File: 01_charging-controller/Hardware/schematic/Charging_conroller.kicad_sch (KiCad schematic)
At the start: 22 parts, among them J1 CAN, J2 SWD, J7 Conn_01x03, J8 Conn_01x03, J9 Conn_01x01, U1 STM32F103CBTx, U2 MCP2562-E-P, U3 L78L33_TO92

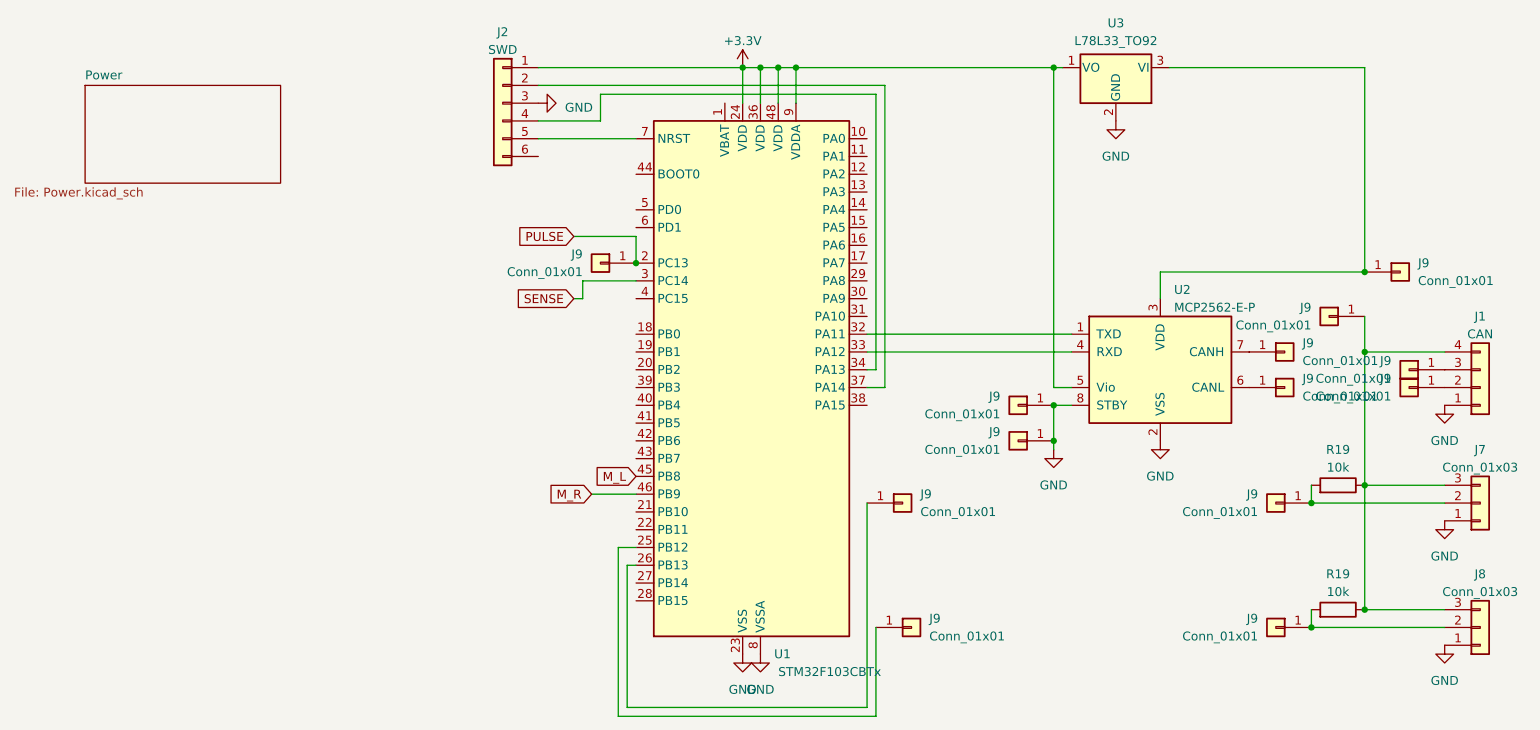
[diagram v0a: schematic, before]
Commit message: minor mistakes fixed; reflected hardware updates
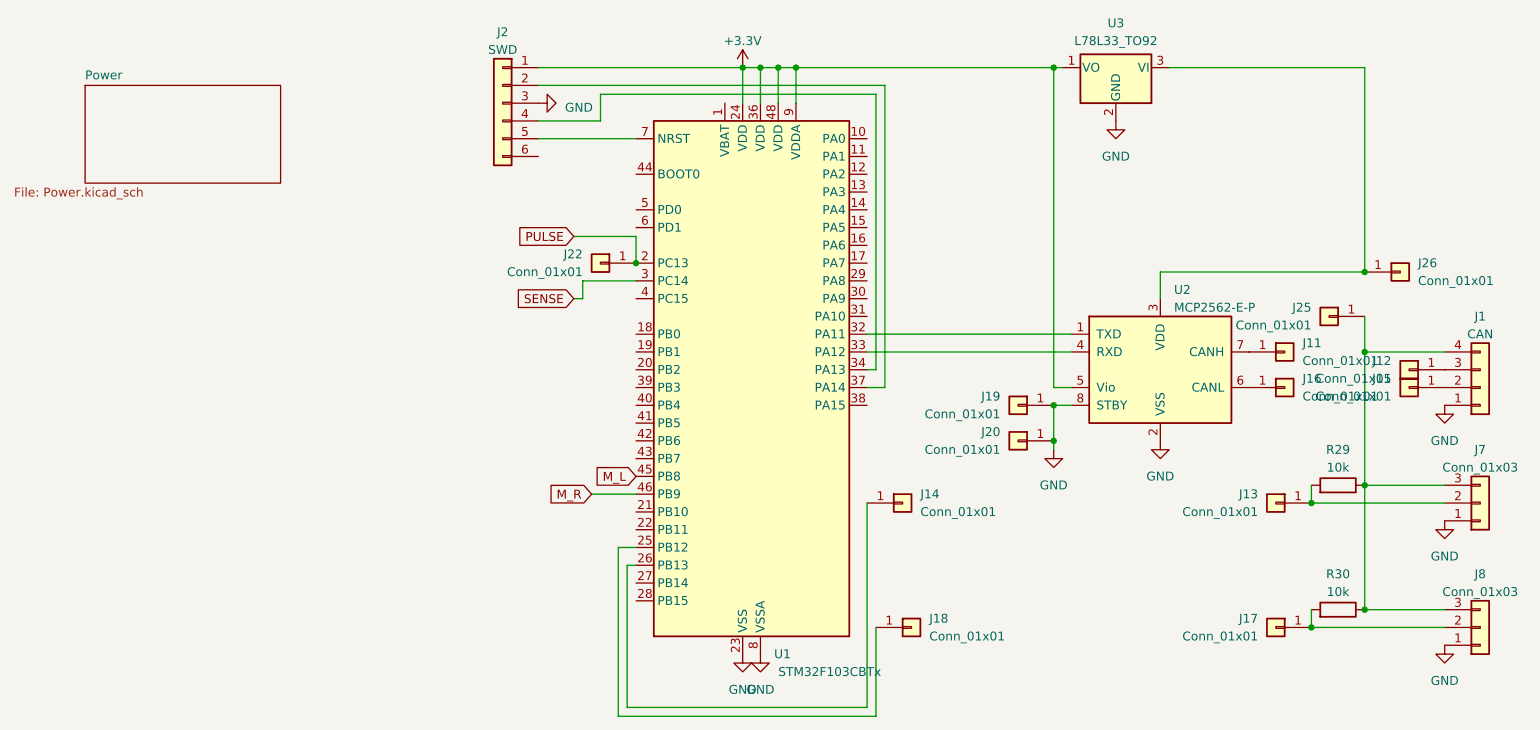
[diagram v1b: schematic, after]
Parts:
- renumbered J9 to J11, J9 to J12, J9 to J13, J9 to J14, J9 to J15, J9 to J16, J9 to J17, J9 to J18, J9 to J19, J9 to J20, J9 to J22, J9 to J25, J9 to J26, R19 to R29, R19 to R30
